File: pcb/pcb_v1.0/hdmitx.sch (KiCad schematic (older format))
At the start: 32 parts, among them J4 HDMI_CONN, U15 TLV70018, U16 TLV70018, U3 IT6613

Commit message: Added ADV7513
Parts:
- added U1: ADV7513, Housings_QFP:LQFP-64_10x10mm_Pitch0.5mm, symbol ADV7513
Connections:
- net labels added: DDCSCL, DDCSDA, TX0+, TX0-, TX1+, TX1-, TX2+, TX2-, TXC+, TXC-
- wire segments 70 -> 117
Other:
- moved on the sheet: C69, C73, C74, C75, C77, C78, C79, C80, C81, C82, C83, C84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

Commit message: Finished power section of ADV7531
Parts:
- removed R25: 698, custom_components:SM0603_Resistor_libcms, symbol R
- removed R26: 1k, custom_components:SM0603_Resistor_libcms, symbol R
- removed U3: IT6613, custom_components:TQFP-100_custom, symbol IT6613
- added C10, C11, C12, C13: 10u, custom_components:SM0603_Capa_libcms, symbol C
- added FB3: MPZ1608S221A, custom_components:SM0603_Resistor_libcms, symbol FILTER
- added R3: 887, custom_components:SM0603_Resistor_libcms, symbol R
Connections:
- net labels added: AVDD1V8, PVDD1V8
- net labels removed: AVCC1V8, AVCC3V3, DDC_SCL, DDC_SDA, DVDD1V8, TMDS_CLK+, TMDS_CLK-, TMDS_D0+, TMDS_D0-, TMDS_D1+, TMDS_D1-, TMDS_D2+, TMDS_D2-
- wire segments 117 -> 93
- no-connect marks 3 -> 8
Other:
- moved on the sheet: C110, C69, C73, C74, C75, C77, C78, C79, C80, C81, C82, C83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

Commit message: initial layout of ADV7513
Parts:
- U1: footprint Housings_QFP:LQFP-64_10x10mm_Pitch0.5mm -> Housings_QFP:LQFP-64-1EP_10x10mm_Pitch0.5mm
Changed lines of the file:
@@
 F 0 "U1" H 3750 6450 50  0000 C CNN
 F 1 "ADV7513" H 3750 6350 50  0000 C CNN
-F 2 "Housings_QFP:LQFP-64_10x10mm_Pitch0.5mm" H 3600 6650 50  0001 C CNN
+F 2 "Housings_QFP:LQFP-64-1EP_10x10mm_Pitch0.5mm" H 3600 6650 50  0001 C CNN
 F 3 "http://www.analog.com/en/products/audio-video/analoghdmidvi-interfaces/analog-hdmidvi-display-interfaces/adv7513.html" H 5450 6550 50  0001 C CNN
 F 4 "Makise Kurisu <kurisu@shimatta.de>" H 3700 6750 50  0001 C CNN "Author"
@@
 F 0 "U1" H 2950 1000 50  0000 C CNN
 F 1 "ADV7513" H 2950 900 50  0000 C CNN
-F 2 "Housings_QFP:LQFP-64_10x10mm_Pitch0.5mm" H 2800 1200 50  0001 C CNN
+F 2 "Housings_QFP:LQFP-64-1EP_10x10mm_Pitch0.5mm" H 2800 1200 50  0001 C CNN
 F 3 "http://www.analog.com/en/products/audio-video/analoghdmidvi-interfaces/analog-hdmidvi-display-interfaces/adv7513.html" H 4650 1100 50  0001 C CNN
 F 4 "Makise Kurisu <kurisu@shimatta.de>" H 2900 1300 50  0001 C CNN "Author"

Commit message: Added Si5351C
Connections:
- net labels added: DVDD1V8
- net labels removed: PVDD1V8
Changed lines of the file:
@@
 LIBS:custom_components
 LIBS:HDMI
+LIBS:74lvc
+LIBS:altera
+LIBS:analog_devices
+LIBS:barrel_jack
+LIBS:battery
+LIBS:beaglebone_black
+LIBS:ck
+LIBS:conn_power
+LIBS:conn_rf
+LIBS:conn_rj
+LIBS:crystal
+LIBS:ddr2_sdram_sodimm
+LIBS:diode
+LIBS:epcos
+LIBS:epcos_dcc6c
+LIBS:fbead
+LIBS:fiducial
+LIBS:freescale_mcu
+LIBS:hackrf_expansion
+LIBS:hdmi
+LIBS:header
+LIBS:hirose
+LIBS:hole
+LIBS:io_expander
+LIBS:lcd_kingtech
+LIBS:ltc
+LIBS:microphone
+LIBS:minicircuits
+LIBS:molex
+LIBS:mosfet
+LIBS:newhaven
+LIBS:noritake
+LIBS:nxp_micro
+LIBS:on_cat24c256
+LIBS:on_semi
+LIBS:osc
+LIBS:passive
+LIBS:regulator
+LIBS:rf_antenna
+LIBS:rf_lna
+LIBS:r_sense
+LIBS:samtec
+LIBS:sd
+LIBS:sharebrained
+LIBS:silabs
+LIBS:supply
+LIBS:switch
+LIBS:terminal_block
+LIBS:ti
+LIBS:ti_cc
+LIBS:tp
+LIBS:trs_jack
+LIBS:usb3_esd_son50-10
+LIBS:usb3_micro_ab
+LIBS:wolfson
 LIBS:cps2_digiav-cache
 EELAYER 25 0
@@
 $Descr A4 11693 8268
 encoding utf-8
-Sheet 2 3
+Sheet 2 4
 Title "CPS2_digiAV"
 Date "2016-09-24"
@@
 $EndComp
 Text Label 10650 5550 0    60   ~ 0
-AVDD1V8
+DVDD1V8
 $Comp
 L TLV71209DBV U16
@@
 $EndComp
 Text Label 10650 6500 0    60   ~ 0
-PVDD1V8
+AVDD1V8
 Text Notes 7000 4100 0    60   ~ 0
 max. 55mA
@@
 $EndComp
 Text Label 8850 5550 0    60   ~ 0
-AVDD3V3
+DVDD3V3
 Text Notes 9800 3100 0    60   ~ 0
 max. 1mA (OVDD)
@@
 Connection ~ 4800 6800
 Text Label 5900 6800 0    60   ~ 0
-PVDD1V8
+AVDD1V8
 Text Label 1200 6400 2    60   ~ 0
-AVDD1V8
+DVDD1V8
 Text Label 1750 6950 2    60   ~ 0
 DVDD3V3

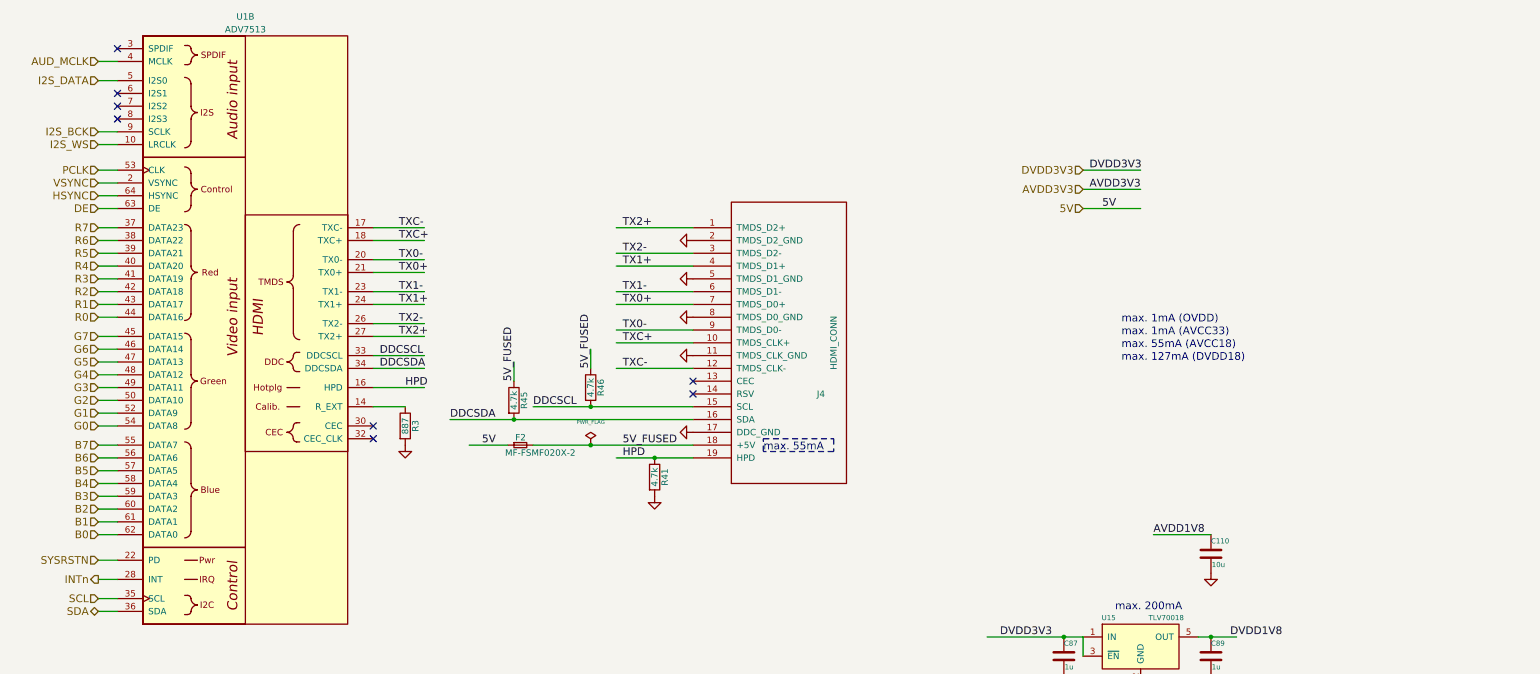
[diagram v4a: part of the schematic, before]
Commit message: Reordered inputs, improved clock layout
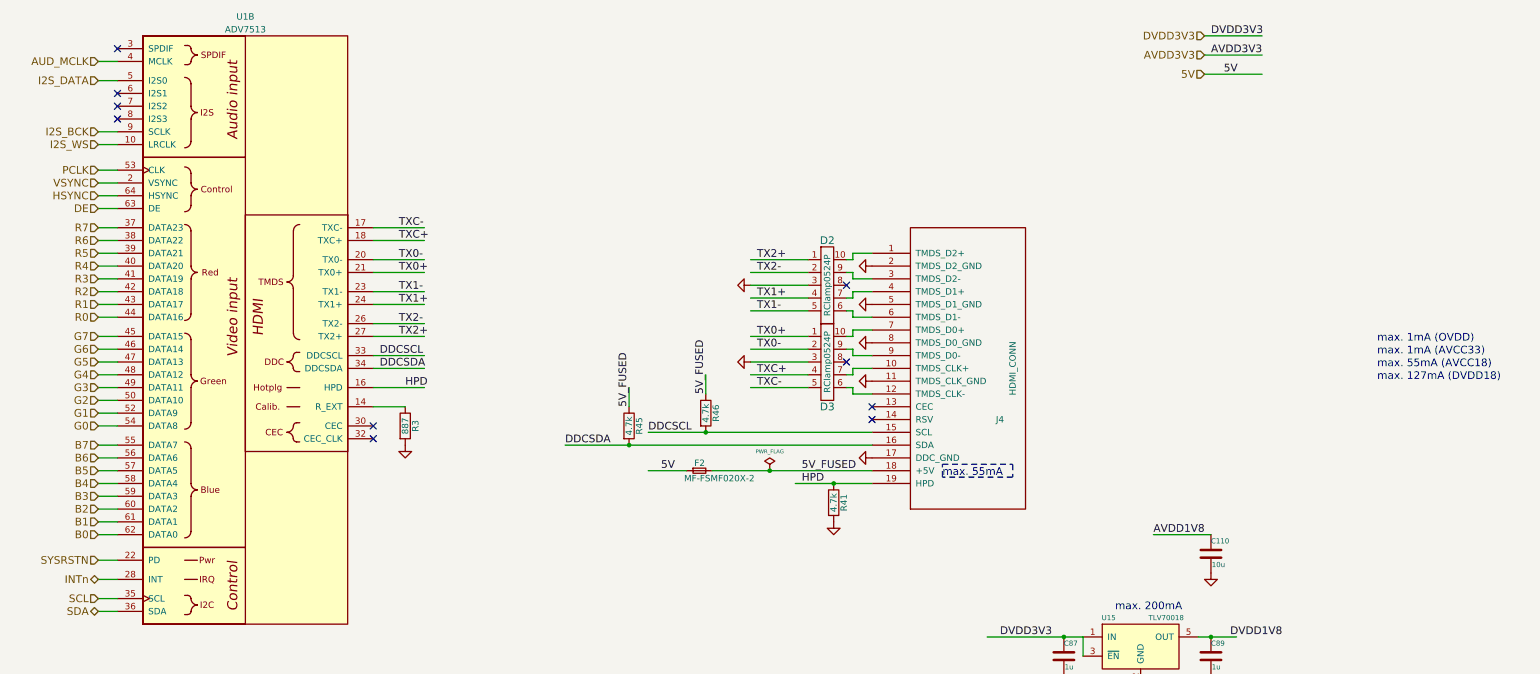
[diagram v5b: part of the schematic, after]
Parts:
- added D2, D3: RClamp0524P, Custom_OSSC:SLP2510P8, symbol RClamp0524P
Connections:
- wire segments 93 -> 119
- no-connect marks 8 -> 10
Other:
- moved on the sheet: F2, J4, R41, R45, R46
